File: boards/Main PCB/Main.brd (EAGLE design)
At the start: 160 x 101.3 mm, 59 parts, among them CN1 MINIB, CN2 MINIB, IC1 FT232RL, IC2 FT232RL, Q1 BSS138, Q2 BSS138, U1 MIC5225-3.3, Y1 32.768kHz

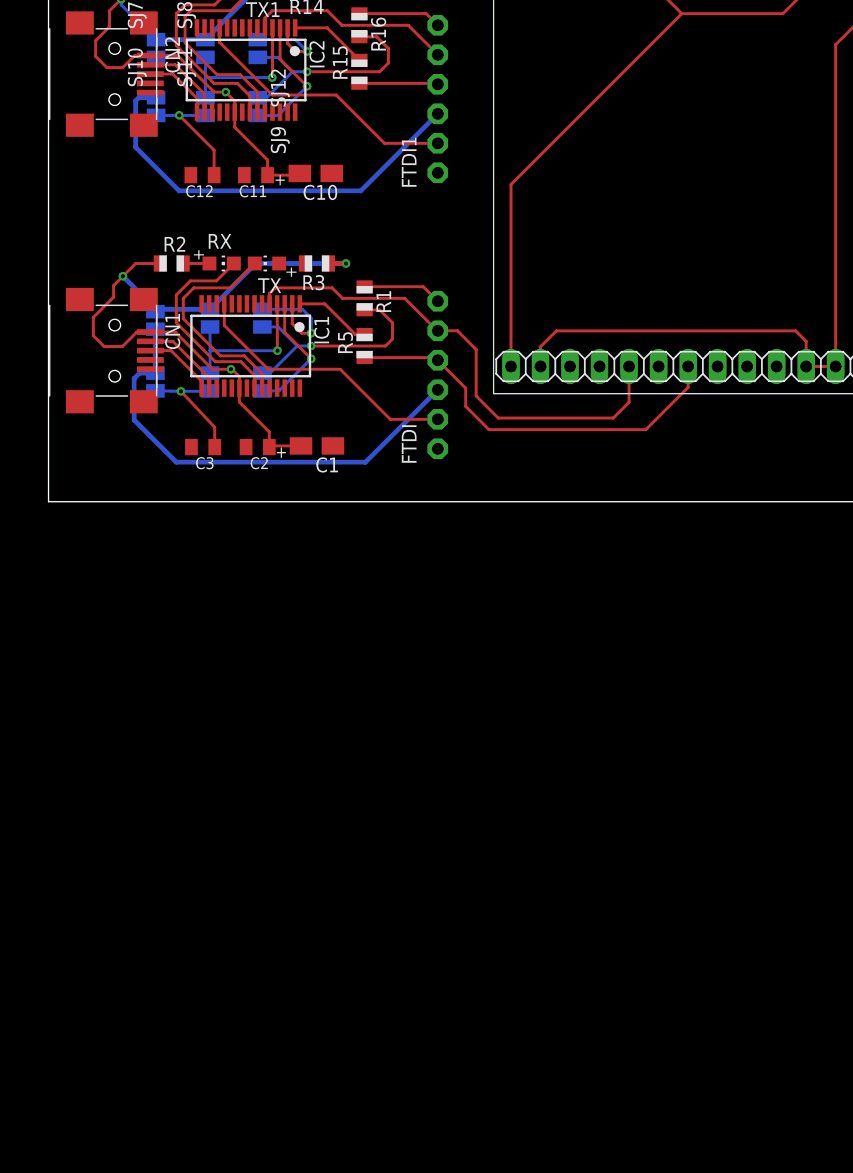
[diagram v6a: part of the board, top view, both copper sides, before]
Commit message: Adding microcontroller to project
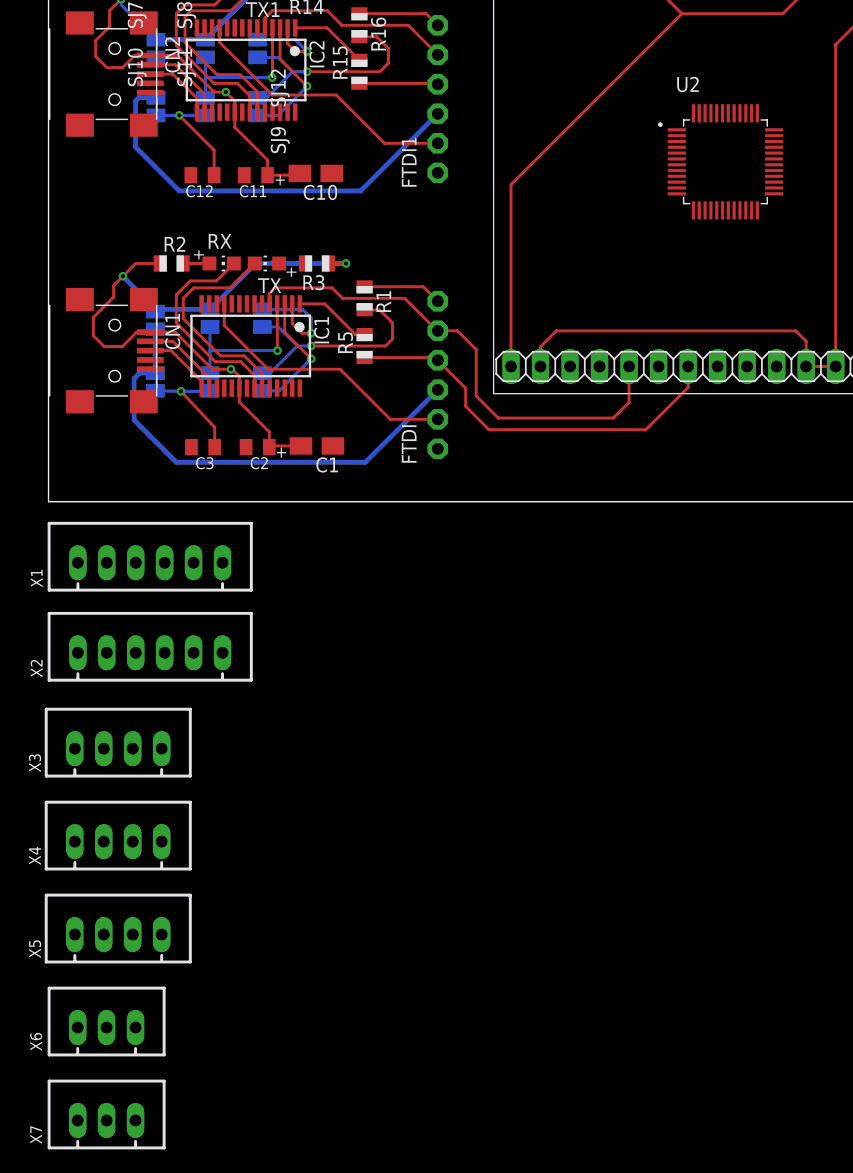
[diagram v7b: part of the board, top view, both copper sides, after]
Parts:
- added U2: STM32F070CBT6, STM32F070CBT6:QFP50P900X900X160-48N
- added X1, X2: JST-XH-06-PIN-LONG-PAD, Rembrandt Electronics - JST XH Connectors v1-0:JST-XH-06-PACKAGE-LONG-PAD
- added X3, X4, X5: JST-XH-04-PIN-LONG-PAD, Rembrandt Electronics - JST XH Connectors v1-0:JST-XH-04-PACKAGE-LONG-PAD
- added X6, X7: JST-XH-03-PIN-LONG-PAD, Rembrandt Electronics - JST XH Connectors v1-0:JST-XH-03-PACKAGE-LONG-PAD
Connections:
- new net N$20: U2.18, X6.2
- new net VDD: U2.1, U2.24, U2.36, U2.48
- new net VDDA: U2.9
- new net VSS: U2.23, U2.35, U2.47
- new net VSSA: U2.8
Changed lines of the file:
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@@
 <drawing>
 <settings>
-<setting alwaysvectorfont="yes"/>
+<setting alwaysvectorfont="no"/>
 <setting verticaltext="up"/>
 </settings>
@@
 <attribute name="VALUE" x="24.464" y="41.762" size="1.27" layer="27" rot="R270"/>
 </element>
+<element name="X1" library="Rembrandt Electronics - JST XH Connectors v1-0" package="JST-XH-06-PACKAGE-LONG-PAD" value="JST-XH-06-PIN-LONG-PAD" x="8.75" y="-5.25" smashed="yes">
+<attribute name="NAME" x="-0.505" y="-7.39" size="1.016" layer="25" ratio="10" rot="R90"/>
+<attribute name="VALUE" x="0.4475" y="-1.3575" size="0.8128" layer="27" ratio="10"/>
+</element>
+<element name="X2" library="Rembrandt Electronics - JST XH Connectors v1-0" package="JST-XH-06-PACKAGE-LONG-PAD" value="JST-XH-06-PIN-LONG-PAD" x="8.75" y="-13" smashed="yes">
+<attribute name="NAME" x="-0.505" y="-15.14" size="1.016" layer="25" ratio="10" rot="R90"/>
+<attribute name="VALUE" x="0.4475" y="-9.1075" size="0.8128" layer="27" ratio="10"/>
+</element>
+<element name="X3" library="Rembrandt Electronics - JST XH Connectors v1-0" package="JST-XH-04-PACKAGE-LONG-PAD" value="JST-XH-04-PIN-LONG-PAD" x="6" y="-21.25" smashed="yes">
+<attribute name="NAME" x="-0.655" y="-23.29" size="1.016" layer="25" ratio="10" rot="R90"/>
+<attribute name="VALUE" x="-0.0025" y="-17.3575" size="1.016" layer="27" ratio="10"/>
+</element>
+<element name="X4" library="Rembrandt Electronics - JST XH Connectors v1-0" package="JST-XH-04-PACKAGE-LONG-PAD" value="JST-XH-04-PIN-LONG-PAD" x="6" y="-29.25" smashed="yes">
+<attribute name="NAME" x="-0.655" y="-31.29" size="1.016" layer="25" ratio="10" rot="R90"/>
+<attribute name="VALUE" x="-0.0025" y="-25.3575" size="1.016" layer="27" ratio="10"/>
+</element>
+<element name="X5" library="Rembrandt Electronics - JST XH Connectors v1-0" package="JST-XH-04-PACKAGE-LONG-PAD" value="JST-XH-04-PIN-LONG-PAD" x="6" y="-37.25" smashed="yes">
+<attribute name="NAME" x="-0.655" y="-39.29" size="1.016" layer="25" ratio="10" rot="R90"/>
+<attribute name="VALUE" x="-0.0025" y="-33.3575" size="1.016" layer="27" ratio="10"/>
+</element>
+<element name="X6" library="Rembrandt Electronics - JST XH Connectors v1-0" package="JST-XH-03-PACKAGE-LONG-PAD" value="JST-XH-03-PIN-LONG-PAD" x="5" y="-45.25" smashed="yes">
+<attribute name="NAME" x="-0.555" y="-47.29" size="1.016" layer="25" ratio="10" rot="R90"/>
+<attribute name="VALUE" x="0.3975" y="-41.3575" size="1.016" layer="27" ratio="10"/>
+</element>
+<element name="X7" library="Rembrandt Electronics - JST XH Connectors v1-0" package="JST-XH-03-PACKAGE-LONG-PAD" value="JST-XH-03-PIN-LONG-PAD" x="5" y="-53.25" smashed="yes">
+<attribute name="NAME" x="-0.555" y="-55.29" size="1.016" layer="25" ratio="10" rot="R90"/>
+<attribute name="VALUE" x="0.3975" y="-49.3575" size="1.016" layer="27" ratio="10"/>
+</element>
+<element name="U2" library="STM32F070CBT6" package="QFP50P900X900X160-48N" value="STM32F070CBT6" x="58.25" y="29.25" smashed="yes">
+<attribute name="DESCRIPTION" value=" Entry-level ARM Cortex-M0 Value line MCU with up to 128 Kbytes Flash, 48 MHz CPU " x="58.25" y="29.25" size="1.778" layer="27" display="off"/>
+<attribute name="DIGI-KEY_PART_NUMBER" value="497-15099-ND" x="58.25" y="29.25" size="1.778" layer="27" display="off"/>
+<attribute name="DIGI-KEY_PURCHASE_URL" value="https://www.digikey.com/product-detail/en/stmicroelectronics/STM32F070CBT6/497-15099-ND/5051734?utm_source=snapeda&amp;utm_medium=aggregator&amp;utm_campaign=symbol" x="58.25" y="29.25" size="1.778" layer="27" display="off"/>
+<attribute name="MF" value="STMicroelectronics" x="58.25" y="29.25" size="1.778" layer="27" display="off"/>
+<attribute name="MP" value="STM32F070CBT6" x="58.25" y="29.25" size="1.778" layer="27" display="off"/>
+<attribute name="NAME" x="53.96435" y="35.266840625" size="1.27433125" layer="25" ratio="10" rot="SR0"/>
+<attribute name="PACKAGE" value="LQFP-48 STMicroelectronics" x="58.25" y="29.25" size="1.778" layer="27" display="off"/>
+<attribute name="VALUE" x="54.35643125" y="22.381190625" size="1.277940625" layer="27" ratio="10" rot="SR0"/>
+</element>
 </elements>
 <signals>
@@
 <wire x1="19.275" y1="36.525" x2="19.25" y2="36.5" width="0.254" layer="1"/>
 </signal>
+<signal name="VDD">
+<contactref element="U2" pad="48"/>
+<contactref element="U2" pad="1"/>
+<contactref element="U2" pad="36"/>
+<contactref element="U2" pad="24"/>
+<wire x1="54.07" y1="32" x2="55.5" y2="33.43" width="0" layer="19" extent="1-1"/>
+<wire x1="62.43" y1="32" x2="55.5" y2="33.43" width="0" layer="19" extent="1-1"/>
+<wire x1="61" y1="25.07" x2="62.43" y2="32" width="0" layer="19" extent="1-1"/>
+</signal>
+<signal name="VDDA">
+<contactref element="U2" pad="9"/>
+</signal>
+<signal name="VSS">
+<contactref element="U2" pad="35"/>
+<contactref element="U2" pad="47"/>
+<contactref element="U2" pad="23"/>
+<wire x1="62.43" y1="31.5" x2="60.5" y2="25.07" width="0" layer="19" extent="1-1"/>
+<wire x1="56" y1="33.43" x2="62.43" y2="31.5" width="0" layer="19" extent="1-1"/>
+</signal>
+<signal name="VSSA">
+<contactref element="U2" pad="8"/>
+</signal>
+<signal name="N$20">
+<contactref element="U2" pad="18"/>
+<contactref element="X6" pad="2"/>
+<wire x1="5" y1="-45.25" x2="58" y2="25.07" width="0" layer="19" extent="1-1"/>
+</signal>
 </signals>
